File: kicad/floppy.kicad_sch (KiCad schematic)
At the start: 15 parts, among them J1 Conn_02x17_Odd_Even, J6 Floppy Power, U1 82077AA/PC8477, Y1 24 MHz

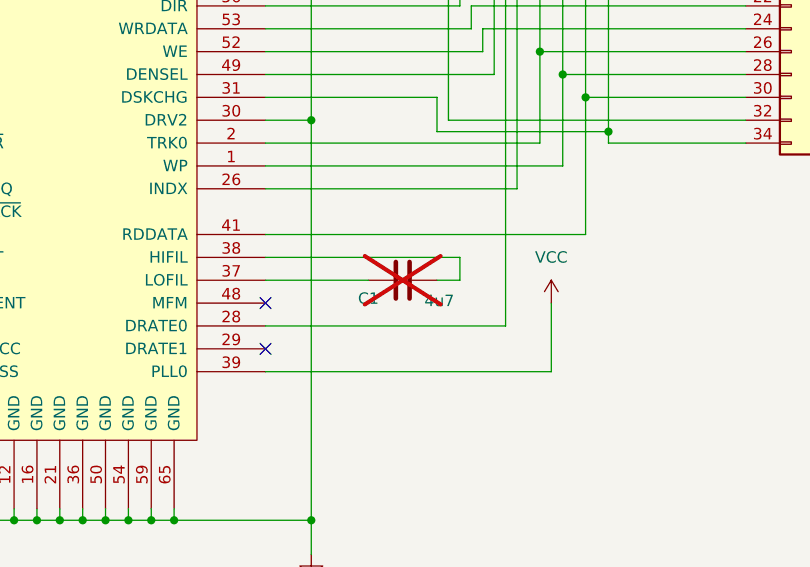
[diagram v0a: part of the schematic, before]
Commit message: HW: Fix unconnected /SOUND net, add /RST header and /DTR power supply
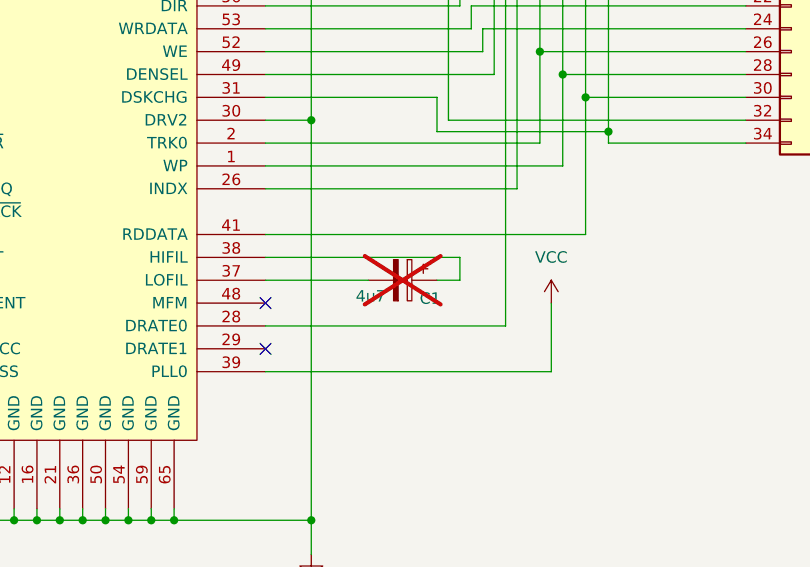
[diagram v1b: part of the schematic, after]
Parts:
- removed C1: 4u7, Capacitor_THT:C_Disc_D4.3mm_W1.9mm_P5.00mm, symbol Device:C
- added C1: 4u7, Capacitor_THT:CP_Radial_D5.0mm_P2.50mm, symbol Device:C_Polarized
- C2, C3: footprint Capacitor_THT:C_Disc_D4.3mm_W1.9mm_P5.00mm -> Capacitor_THT:C_Disc_D5.0mm_W2.5mm_P2.50mm
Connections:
- net at U1.37 (LOFIL): now also C1.2
- net at U1.38 (HIFIL): now also C1.1
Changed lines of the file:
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@@
 			)
 		)
-		(property "Footprint" "Capacitor_THT:C_Disc_D4.3mm_W1.9mm_P5.00mm"
+		(property "Footprint" "Capacitor_THT:C_Disc_D5.0mm_W2.5mm_P2.50mm"
 			(at 76.5048 63.5 0)
 			(effects
@@
 	)
 	(symbol
-		(lib_id "Device:C")
-		(at 162.56 124.46 90)
-		(unit 1)
-		(exclude_from_sim no)
-		(in_bom yes)
-		(on_board yes)
-		(dnp yes)
-		(property "Reference" "C1"
-			(at 158.75 126.492 90)
-			(effects
-				(font
-					(size 1.27 1.27)
-				)
-			)
-		)
-		(property "Value" "4u7"
-			(at 166.624 126.746 90)
-			(effects
-				(font
-					(size 1.27 1.27)
-				)
-			)
-		)
-		(property "Footprint" "Capacitor_THT:C_Disc_D4.3mm_W1.9mm_P5.00mm"
-			(at 166.37 123.4948 0)
-			(effects
-				(font
-					(size 1.27 1.27)
-				)
-				(hide yes)
-			)
-		)
-		(property "Datasheet" "~"
-			(at 162.56 124.46 0)
-			(effects
-				(font
-					(size 1.27 1.27)
-				)
-				(hide yes)
-			)
-		)
-		(property "Description" "Unpolarized capacitor"
-			(at 162.56 124.46 0)
-			(effects
-				(font
-					(size 1.27 1.27)
-				)
-				(hide yes)
-			)
-		)
-		(pin "1"
-		)
-		(pin "2"
-		)
-		(instances
-			(project ""
-				(path "/ca48b56d-33a4-442b-b1b9-aaf2c2c8d68d/60a54ca7-49fc-4005-bb61-fc7fc4ae3170"
-					(reference "C1")
-					(unit 1)
-				)
-			)
-		)
-	)
-	(symbol
 		(lib_id "power:VCC")
 		(at 66.04 132.08 0)
@@
 	)
 	(symbol
+		(lib_id "Device:C_Polarized")
+		(at 162.56 124.46 270)
+		(unit 1)
+		(exclude_from_sim no)
+		(in_bom yes)
+		(on_board yes)
+		(dnp yes)
+		(property "Reference" "C1"
+			(at 165.608 126.492 90)
+			(effects
+				(font
+					(size 1.27 1.27)
+				)
+			)
+		)
+		(property "Value" "4u7"
+			(at 159.004 126.238 90)
+			(effects
+				(font
+					(size 1.27 1.27)
+				)
+			)
+		)
+		(property "Footprint" "Capacitor_THT:CP_Radial_D5.0mm_P2.50mm"
+			(at 158.75 125.4252 0)
+			(effects
+				(font
+					(size 1.27 1.27)
+				)
+				(hide yes)
+			)
+		)
+		(property "Datasheet" "~"
+			(at 162.56 124.46 0)
+			(effects
+				(font
+					(size 1.27 1.27)
+				)
+				(hide yes)
+			)
+		)
+		(property "Description" "Polarized capacitor"
+			(at 162.56 124.46 0)
+			(effects
+				(font
+					(size 1.27 1.27)
+				)
+				(hide yes)
+			)
+		)
+		(pin "1"
+		)
+		(pin "2"
+		)
+		(instances
+			(project "zak180"
+				(path "/ca48b56d-33a4-442b-b1b9-aaf2c2c8d68d/60a54ca7-49fc-4005-bb61-fc7fc4ae3170"
+					(reference "C1")
+					(unit 1)
+				)
+			)
+		)
+	)
+	(symbol
 		(lib_id "Device:Crystal")
 		(at 69.85 60.96 0)
@@
 			)
 		)
-		(property "Footprint" "Capacitor_THT:C_Disc_D4.3mm_W1.9mm_P5.00mm"
+		(property "Footprint" "Capacitor_THT:C_Disc_D5.0mm_W2.5mm_P2.50mm"
 			(at 61.2648 63.5 0)
 			(effects
